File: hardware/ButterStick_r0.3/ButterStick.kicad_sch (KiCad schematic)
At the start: 3 parts

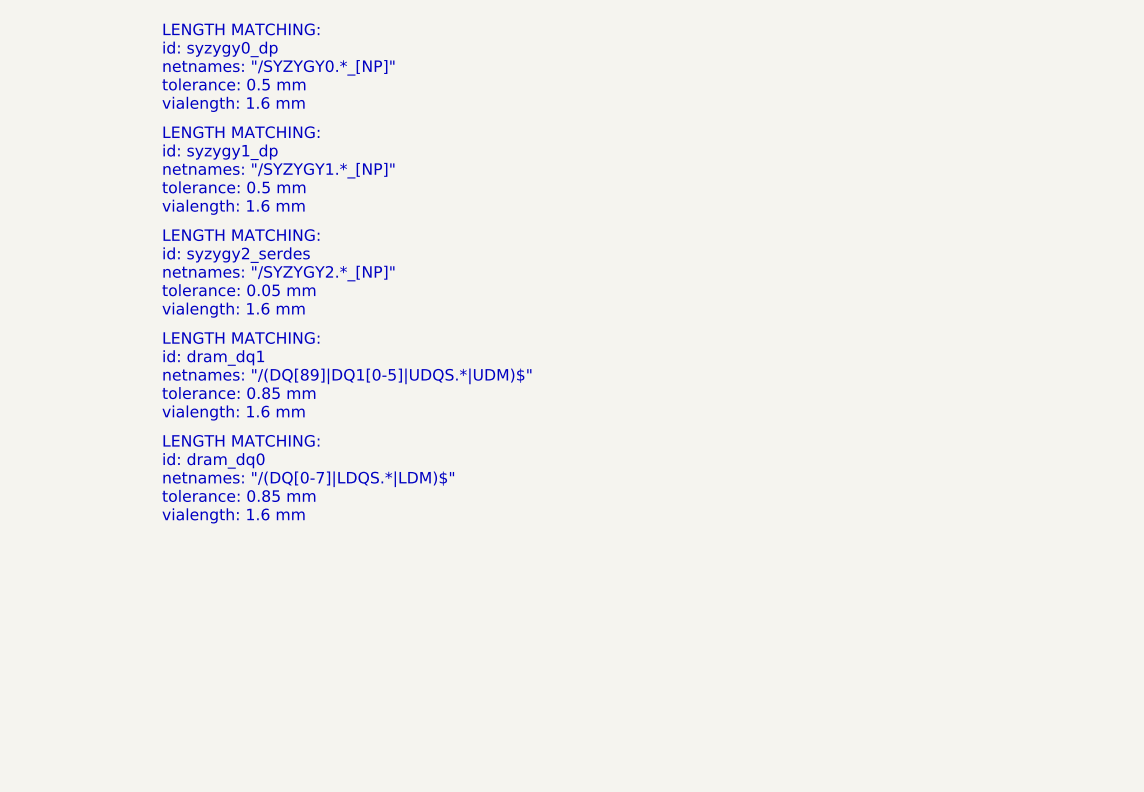
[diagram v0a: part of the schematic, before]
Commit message: hw.r0d3: update DDR3 pinmap and routing
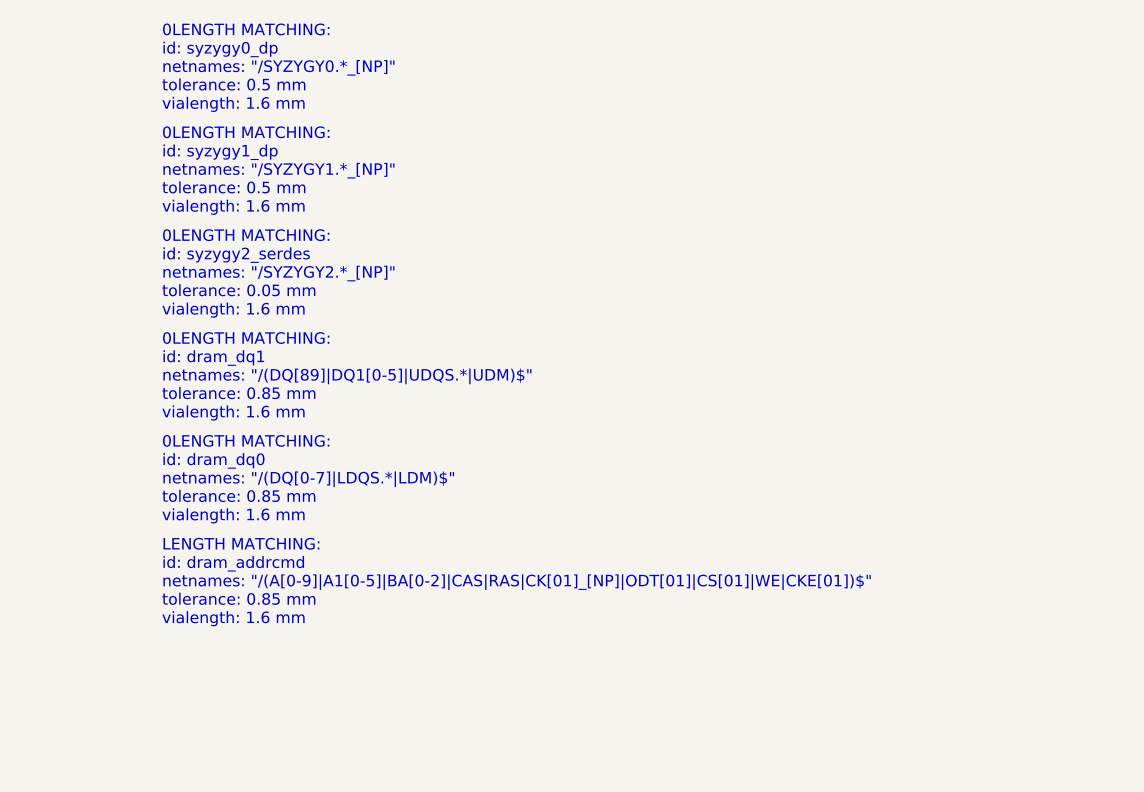
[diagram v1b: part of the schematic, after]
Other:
- note added: "0LENGTH MATCHING: id: dram_dq0 netnames: "/(DQ[0-7]|LDQS.*|LDM)$" tolerance: 0.85 mm vialength: 1.6 mm"
- note added: "0LENGTH MATCHING: id: dram_dq1 netnames: "/(DQ[89]|DQ1[0-5]|UDQS.*|UDM)$" tolerance: 0.85 mm vialength: 1.6 mm"
- note added: "0LENGTH MATCHING: id: syzygy0_dp netnames: "/SYZYGY0.*_[NP]" tolerance: 0.5 mm vialength: 1.6 mm"
- note added: "0LENGTH MATCHING: id: syzygy1_dp netnames: "/SYZYGY1.*_[NP]" tolerance: 0.5 mm vialength: 1.6 mm"
- note added: "0LENGTH MATCHING: id: syzygy2_serdes netnames: "/SYZYGY2.*_[NP]" tolerance: 0.05 mm vialength: 1.6 mm"
- note added: "LENGTH MATCHING: id: dram_addrcmd netnames: "/(A[0-9]|A1[0-5]|BA[0-2]|CAS|RAS|CK[01]_[NP]|ODT[01]|CS[01]|WE|CKE[01])$" tolerance: 0.85 mm vialength: 1.6 mm"
- note removed: "LENGTH MATCHING: id: dram_dq0 netnames: "/(DQ[0-7]|LDQS.*|LDM)$" tolerance: 0.85 mm vialength: 1.6 mm"
- note removed: "LENGTH MATCHING: id: dram_dq1 netnames: "/(DQ[89]|DQ1[0-5]|UDQS.*|UDM)$" tolerance: 0.85 mm vialength: 1.6 mm"
- note removed: "LENGTH MATCHING: id: syzygy0_dp netnames: "/SYZYGY0.*_[NP]" tolerance: 0.5 mm vialength: 1.6 mm"
- note removed: "LENGTH MATCHING: id: syzygy1_dp netnames: "/SYZYGY1.*_[NP]" tolerance: 0.5 mm vialength: 1.6 mm"
- note removed: "LENGTH MATCHING: id: syzygy2_serdes netnames: "/SYZYGY2.*_[NP]" tolerance: 0.05 mm vialength: 1.6 mm"

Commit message: hw.r0d3: complete first pass of routing
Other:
- sheet FPGA-MISC ports: added SDMMC0{SDMMC}; removed none
- sheet sheetFPGA ports: added {LED[0..6] LEDC[0..2]}, {PDM[0..2]}; removed none
- sheet sheetIO ports: added SDMMC0{SDMMC}; removed none
- note added: "LENGTH MATCHING: id: dram_addrcmd netnames: "/(A[0-9]|A1[0-5]|BA[0-2]|CAS|RAS|WE)$" tolerance: 0.85 mm vialength: 1.6 mm"
- note added: "LENGTH MATCHING: id: dram_addrcmd netnames: "/(CK[01]_[NP]|ODT[01]|CS[01]|CKE[01])$" tolerance: 0.85 mm vialength: 1.6 mm"
- note added: "LENGTH MATCHING: id: dram_dq0 netnames: "/(DQ[0-7]|LDQS.*|LDM)$" tolerance: 0.85 mm vialength: 1.6 mm"
- note added: "LENGTH MATCHING: id: dram_dq1 netnames: "/(DQ[89]|DQ1[0-5]|UDQS.*|UDM)$" tolerance: 0.85 mm vialength: 1.6 mm"
- note added: "LENGTH MATCHING: id: syzygy0_dp netnames: "/SYZYGY0.*_[NP]" tolerance: 0.5 mm vialength: 1.6 mm"
- note added: "LENGTH MATCHING: id: syzygy1_dp netnames: "/SYZYGY1.*_[NP]" tolerance: 0.5 mm vialength: 1.6 mm"
- note added: "LENGTH MATCHING: id: syzygy2_serdes netnames: "/SYZYGY2.*_[NP]" tolerance: 0.05 mm vialength: 1.6 mm"
- note removed: "0LENGTH MATCHING: id: dram_dq0 netnames: "/(DQ[0-7]|LDQS.*|LDM)$" tolerance: 0.85 mm vialength: 1.6 mm"
- note removed: "0LENGTH MATCHING: id: dram_dq1 netnames: "/(DQ[89]|DQ1[0-5]|UDQS.*|UDM)$" tolerance: 0.85 mm vialength: 1.6 mm"
- note removed: "0LENGTH MATCHING: id: syzygy0_dp netnames: "/SYZYGY0.*_[NP]" tolerance: 0.5 mm vialength: 1.6 mm"
- note removed: "0LENGTH MATCHING: id: syzygy1_dp netnames: "/SYZYGY1.*_[NP]" tolerance: 0.5 mm vialength: 1.6 mm"
- note removed: "0LENGTH MATCHING: id: syzygy2_serdes netnames: "/SYZYGY2.*_[NP]" tolerance: 0.05 mm vialength: 1.6 mm"
- note removed: "LENGTH MATCHING: id: dram_addrcmd netnames: "/(A[0-9]|A1[0-5]|BA[0-2]|CAS|RAS|CK[01]_[NP]|ODT[01]|CS[01]|WE|CKE[01])$" tolerance: 0.85 mm vialength: 1.6 mm"

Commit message: hw.r0d3: Tweaking routing
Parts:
- added H1, H2: MountingHole, MountingHole:MountingHole_3.2mm_M3_Pad_Via, symbol Mechanical:MountingHole
- added LOGO1: Q_NMOS_GSD, gkl_logos:gsd_logo_small, symbol Device:Q_NMOS_GSD
- added LOGO2: Logo_Open_Hardware_Small, gkl_logos:oshw_small, symbol Graphic:Logo_Open_Hardware_Small

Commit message: hw.r0d3: Small routing tweaks
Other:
- removed sheet TestPoints
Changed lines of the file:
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@@
 (kicad_sch (version 20200618) (host eeschema "5.99.0-unknown-73168a9~101~ubuntu18.04.1")
-  (page 1 19)
+  (page 1 18)
   (paper "A4")
   (title_block
@@
     (company "GsD")
   )
+  (bus_alias "SYZYGY_STD" (members "D0_P" "D0_N" "D2_P" "D2_N" "D4_P" "D4_N" "D6_P" "D6_N" "S16" "S18" "S20" "S22" "S24" "S26" "P2C_CLK_P" "P2C_CLK_N" "VIO1" "R_GA" "D1_P" "D1_N" "D3_P" "D3_N" "D5_P" "D5_N" "D7_P" "D7_N" "S17" "S19" "S21" "S23" "S25" "S27" "C2P_CLK_P" "C2P_CLK_N"))
+  (bus_alias "RGMII" (members "RESET" "MDC" "MDIO" "TX[0..3]" "RX[0..3]" "TX_CTRL" "TX_CLK" "RX_CTRL" "RX_CLK" "INT" "CLK125"))
   (bus_alias "SDMMC" (members "DAT[0..3]" "CMD" "CK" "CD"))
+  (bus_alias "SYZYGY_TXR4" (members "RX0_P" "RX0_N" "RX1_P" "RX1_N" "REFCLK_P" "REFCLK_N" "S2" "S4" "S6" "S8" "RX3_P" "RX3_N" "RX2_P" "RX2_N" "P2C_CLK_P" "P2C_CLK_N" "VIO1" "R_GA" "TX0_P" "TX0_N" "TX1_P" "TX1_N" "S0" "S1" "S3" "S5" "S7" "S9" "TX3_P" "TX3_N" "TX2_P" "TX2_N" "C2P_CLK_P" "C2P_CLK_N"))
   (bus_alias "ULPI" (members "DATA[0..7]" "STP" "NXT" "DIR" "RESET" "REFCLK"))
-  (bus_alias "SYZYGY_TXR4" (members "RX0_P" "RX0_N" "RX1_P" "RX1_N" "REFCLK_P" "REFCLK_N" "S2" "S4" "S6" "S8" "RX3_P" "RX3_N" "RX2_P" "RX2_N" "P2C_CLK_P" "P2C_CLK_N" "VIO1" "R_GA" "TX0_P" "TX0_N" "TX1_P" "TX1_N" "S0" "S1" "S3" "S5" "S7" "S9" "TX3_P" "TX3_N" "TX2_P" "TX2_N" "C2P_CLK_P" "C2P_CLK_N"))
   (bus_alias "I2C" (members "SDA" "SCL"))
   (bus_alias "DRAM_DAT" (members "DQ[15..0]" "LDQS_P" "LDQS_N" "UDQS_P" "UDQS_N"))
   (bus_alias "DRAM_CTRL" (members "A[15..0]" "BA[2..0]" "LDM" "UDM" "ODT[0..1]" "RAS" "CAS" "WE" "CK0_P" "CK0_N" "CKE[0..1]" "CS[0..1]" "CK1_N" "CK1_P" "RST"))
-  (bus_alias "RGMII" (members "RESET" "MDC" "MDIO" "TX[0..3]" "RX[0..3]" "TX_CTRL" "TX_CLK" "RX_CTRL" "RX_CLK" "INT" "CLK125"))
-  (bus_alias "SYZYGY_STD" (members "D0_P" "D0_N" "D2_P" "D2_N" "D4_P" "D4_N" "D6_P" "D6_N" "S16" "S18" "S20" "S22" "S24" "S26" "P2C_CLK_P" "P2C_CLK_N" "VIO1" "R_GA" "D1_P" "D1_N" "D3_P" "D3_N" "D5_P" "D5_N" "D7_P" "D7_N" "S17" "S19" "S21" "S23" "S25" "S27" "C2P_CLK_P" "C2P_CLK_N"))
   (junction (at 180.34 105.41) (diameter 0) (color 0 0 0 0))
   (junction (at 180.34 124.46) (diameter 0) (color 0 0 0 0))
@@
     )
   )
-  (sheet (at 314.96 154.94) (size 46.99 24.13)
-    (stroke (width 0.1524) (type solid) (color 132 0 132 1))
-    (fill (color 255 255 255 1.0000))
-    (property "Sheet name" "TestPoints" (id 0) (at 314.96 154.3045 0)
-      (effects (font (size 1.27 1.27)) (justify left bottom))
-    )
-    (property "Sheet file" "TestPonts.kicad_sch" (id 1) (at 314.96 179.5785 0)
-      (effects (font (size 1.27 1.27)) (justify left top))
-    )
-  )
   (sheet (at 44.45 72.39) (size 24.13 12.7)
     (stroke (width 0.1524) (type solid) (color 132 0 132 1))
@@
       (reference "#PWR0217") (unit 1)
     )
-    (path "/f9addc60-22bd-459e-944d-bb7e5f89424d/c6c86e84-fe9b-427f-b86f-a3fd246d01f9"
+    (path "/f9addc60-22bd-459e-944d-bb7e5f89424d/40acb536-c6a0-4e3d-b43d-330466c07d96"
       (reference "#PWR0218") (unit 1)
     )
@@
       (reference "#PWR0232") (unit 1)
     )
-    (path "/f9addc60-22bd-459e-944d-bb7e5f89424d/633b0eff-f7ce-4dd3-bcb4-c347c5835db6"
+    (path "/f9addc60-22bd-459e-944d-bb7e5f89424d/99bdac1e-b3ae-4938-988c-51fed9e8b1c0"
       (reference "#PWR0233") (unit 1)
     )
@@
       (reference "#PWR0163") (unit 1)
     )
+    (path "/8c5c97be-ac2a-423b-b313-79cf2d3690d4/ab00729b-e68f-45fe-a8b8-66d90dcbc74c/c3a38a79-19ea-424e-ac2b-e7fb2dd7756a"
+      (reference "#PWR0236") (unit 1)
+    )
+    (path "/8c5c97be-ac2a-423b-b313-79cf2d3690d4/ab00729b-e68f-45fe-a8b8-66d90dcbc74c/d3e6102e-e397-406d-a155-d99025e6e81e"
+      (reference "#PWR0238") (unit 1)
+    )
+    (path "/8c5c97be-ac2a-423b-b313-79cf2d3690d4/ab00729b-e68f-45fe-a8b8-66d90dcbc74c/39099011-daa9-4cf0-b6a2-77456c2a8409"
+      (reference "#PWR0239") (unit 1)
+    )
     (path "/8c5c97be-ac2a-423b-b313-79cf2d3690d4/ab00729b-e68f-45fe-a8b8-66d90dcbc74c/3a2dd779-b92b-424e-891f-3969e2e44718"
       (reference "C21") (unit 1)
@@
       (reference "C120") (unit 1)
     )
+    (path "/8c5c97be-ac2a-423b-b313-79cf2d3690d4/ab00729b-e68f-45fe-a8b8-66d90dcbc74c/e486cc46-06c3-4fe3-87ce-fcf2a2f39a4f"
+      (reference "C145") (unit 1)
+    )
+    (path "/8c5c97be-ac2a-423b-b313-79cf2d3690d4/ab00729b-e68f-45fe-a8b8-66d90dcbc74c/6db63fd6-3c8c-4ae1-9b82-de1fceb72bfe"
+      (reference "C147") (unit 1)
+    )
+    (path "/8c5c97be-ac2a-423b-b313-79cf2d3690d4/ab00729b-e68f-45fe-a8b8-66d90dcbc74c/ec4cde8b-7d0a-42e6-a9ff-b7c5be8f7e47"
+      (reference "C148") (unit 1)
+    )
     (path "/8c5c97be-ac2a-423b-b313-79cf2d3690d4/ab00729b-e68f-45fe-a8b8-66d90dcbc74c/888ee4f1-f16d-4a35-afa0-fcb64314ad36"
       (reference "R67") (unit 1)
@@
       (reference "R68") (unit 1)
     )
+    (path "/8c5c97be-ac2a-423b-b313-79cf2d3690d4/ab00729b-e68f-45fe-a8b8-66d90dcbc74c/8be4c673-e88b-41d2-9e59-b60795aede15"
+      (reference "R93") (unit 1)
+    )
     (path "/8c5c97be-ac2a-423b-b313-79cf2d3690d4/ab00729b-e68f-45fe-a8b8-66d90dcbc74c/55f8581f-8a50-4243-9b7c-67e348100131"
       (reference "U11") (unit 1)
@@
       (reference "#PWR0209") (unit 1)
     )
+    (path "/8c5c97be-ac2a-423b-b313-79cf2d3690d4/3fb004e8-3d03-4814-9e49-7690a14dd4d7/c3a38a79-19ea-424e-ac2b-e7fb2dd7756a"
+      (reference "#PWR0237") (unit 1)
+    )
+    (path "/8c5c97be-ac2a-423b-b313-79cf2d3690d4/3fb004e8-3d03-4814-9e49-7690a14dd4d7/d3e6102e-e397-406d-a155-d99025e6e81e"
+      (reference "#PWR0240") (unit 1)
+    )
+    (path "/8c5c97be-ac2a-423b-b313-79cf2d3690d4/3fb004e8-3d03-4814-9e49-7690a14dd4d7/39099011-daa9-4cf0-b6a2-77456c2a8409"
+      (reference "#PWR0241") (unit 1)
+    )
     (path "/8c5c97be-ac2a-423b-b313-79cf2d3690d4/3fb004e8-3d03-4814-9e49-7690a14dd4d7/3a2dd779-b92b-424e-891f-3969e2e44718"
       (reference "C22") (unit 1)
@@
       (reference "C121") (unit 1)
     )
+    (path "/8c5c97be-ac2a-423b-b313-79cf2d3690d4/3fb004e8-3d03-4814-9e49-7690a14dd4d7/e486cc46-06c3-4fe3-87ce-fcf2a2f39a4f"
+      (reference "C146") (unit 1)
+    )
+    (path "/8c5c97be-ac2a-423b-b313-79cf2d3690d4/3fb004e8-3d03-4814-9e49-7690a14dd4d7/6db63fd6-3c8c-4ae1-9b82-de1fceb72bfe"
+      (reference "C149") (unit 1)
+    )
+    (path "/8c5c97be-ac2a-423b-b313-79cf2d3690d4/3fb004e8-3d03-4814-9e49-7690a14dd4d7/ec4cde8b-7d0a-42e6-a9ff-b7c5be8f7e47"
+      (reference "C150") (unit 1)
+    )
     (path "/8c5c97be-ac2a-423b-b313-79cf2d3690d4/3fb004e8-3d03-4814-9e49-7690a14dd4d7/888ee4f1-f16d-4a35-afa0-fcb64314ad36"
       (reference "R71") (unit 1)
@@
       (reference "R72") (unit 1)
     )
+    (path "/8c5c97be-ac2a-423b-b313-79cf2d3690d4/3fb004e8-3d03-4814-9e49-7690a14dd4d7/8be4c673-e88b-41d2-9e59-b60795aede15"
+      (reference "R94") (unit 1)
+    )
     (path "/8c5c97be-ac2a-423b-b313-79cf2d3690d4/3fb004e8-3d03-4814-9e49-7690a14dd4d7/55f8581f-8a50-4243-9b7c-67e348100131"

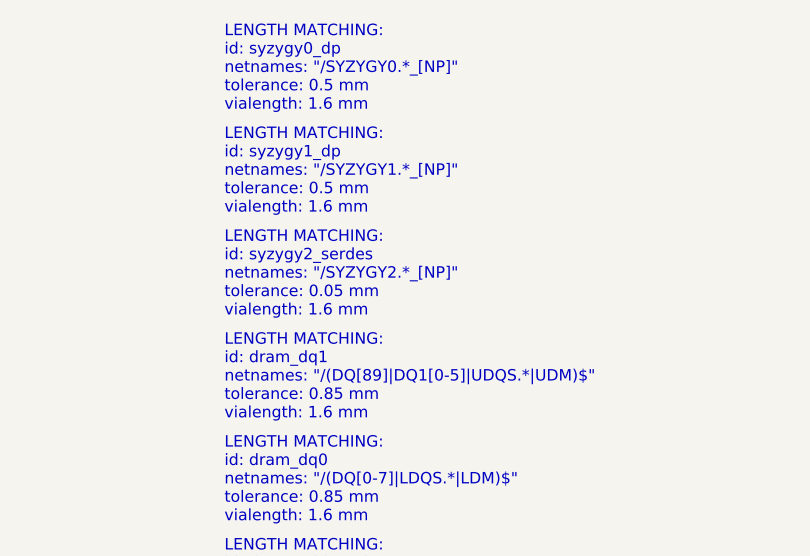
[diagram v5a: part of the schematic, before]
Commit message: hw.r0d3: tweak length matching
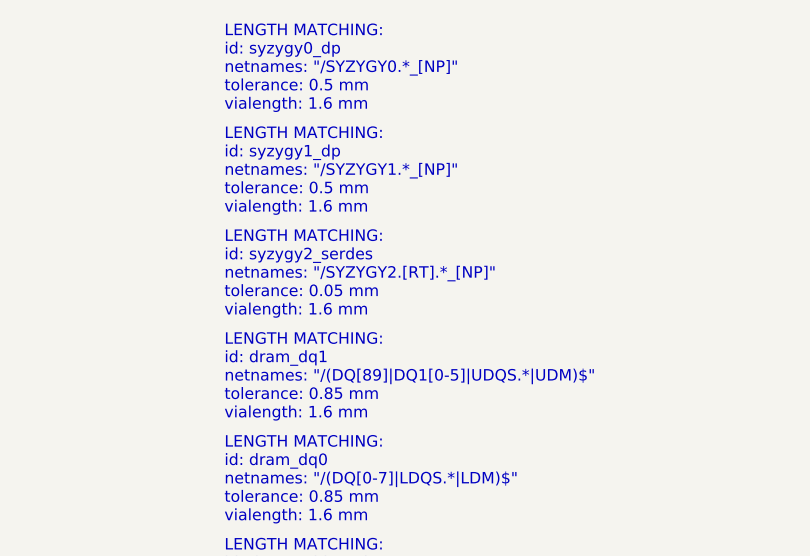
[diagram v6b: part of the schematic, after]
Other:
- note added: "LENGTH MATCHING: id: syzygy2_serdes netnames: "/SYZYGY2.[RT].*_[NP]" tolerance: 0.05 mm vialength: 1.6 mm"
- note removed: "LENGTH MATCHING: id: syzygy2_serdes netnames: "/SYZYGY2.*_[NP]" tolerance: 0.05 mm vialength: 1.6 mm"
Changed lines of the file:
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@@
     (effects (font (size 1.27 1.27)) (justify left bottom))
   )
-  (text "LENGTH MATCHING:\nid: syzygy2_serdes\nnetnames: \"/SYZYGY2.*_[NP]\"\ntolerance: 0.05 mm\nvialength: 1.6 mm"
+  (text "LENGTH MATCHING:\nid: syzygy2_serdes\nnetnames: \"/SYZYGY2.[RT].*_[NP]\"\ntolerance: 0.05 mm\nvialength: 1.6 mm"
     (at 300.99 35.56 0)
     (effects (font (size 1.27 1.27)) (justify left bottom))
